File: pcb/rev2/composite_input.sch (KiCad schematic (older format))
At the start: 19 parts, among them IC28 TVP5150AM1PBS, X1 XTAL_12MHZ_TXC_7A-14.31818MAA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

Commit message: pcb wip
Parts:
- C29, C30, C31, C52, C59, C83: footprint CAPC1608X87N -> Capacitors SMD:CAPC1608X87N
- C7, C84, C85, C86: footprint CAPC1608X90N -> Capacitors SMD:CAPC1608X90N
- L1, L6: footprint INDC2012X105N -> Inductors SMD:INDC2012X105N
- R19, R32, R33, R4, R48: footprint RESC1608X55N -> Resistors SMD:RESC1608X55N
- X1: footprint XTAL_TXC_7A -> ICs And Semiconductors SMD:XTAL_TXC_7A
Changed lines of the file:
@@
 F 0 "R19" H 2050 1697 50  0000 C CNN
 F 1 "R0603_33R_1%_0.1W_100PPM" H 1900 1290 60  0001 L CNN
-F 2 "RESC1608X55N" H 1900 480 60  0001 L CNN
+F 2 "Resistors SMD:RESC1608X55N" H 1900 480 60  0001 L CNN
 F 3 "\\cern.ch\\dfs\\Applications\\Altium\\Datasheets\\R0603_NIC_NRC.pdf" H 1900 1110 60  0001 L CNN
 F 4 "33" H 2050 1606 50  0000 C CNN "~"
@@
 F 0 "R32" V 2404 1660 50  0000 L CNN
 F 1 "R0603_33R_1%_0.1W_100PPM" H 2300 1390 60  0001 L CNN
-F 2 "RESC1608X55N" H 2300 580 60  0001 L CNN
+F 2 "Resistors SMD:RESC1608X55N" H 2300 580 60  0001 L CNN
 F 3 "\\cern.ch\\dfs\\Applications\\Altium\\Datasheets\\R0603_NIC_NRC.pdf" H 2300 1210 60  0001 L CNN
 F 4 "33" V 2495 1660 50  0000 L CNN "~"
@@
 F 0 "C7" H 2600 1747 50  0000 C CNN
 F 1 "CC0603_100NF_100V_10%_X7R" H 2450 1240 60  0001 L CNN
-F 2 "CAPC1608X90N" H 2450 430 60  0001 L CNN
+F 2 "Capacitors SMD:CAPC1608X90N" H 2450 430 60  0001 L CNN
 F 3 "\\cern.ch\\dfs\\Applications\\Altium\\Datasheets\\CC0603_MURATA_GRM188R72A104KA35D.pdf" H 2450 1060 60  0001 L CNN
 F 4 "100nF" H 2600 1656 50  0000 C CNN "~"
@@
 F 0 "R33" H 4400 3297 50  0000 C CNN
 F 1 "R0603_3K3_1%_0.1W_100PPM" H 4250 2890 60  0001 L CNN
-F 2 "RESC1608X55N" H 4250 2080 60  0001 L CNN
+F 2 "Resistors SMD:RESC1608X55N" H 4250 2080 60  0001 L CNN
 F 3 "\\cern.ch\\dfs\\Applications\\Altium\\Datasheets\\R0603_NIC_NRC.pdf" H 4250 2710 60  0001 L CNN
 F 4 "3k3" H 4400 3206 50  0000 C CNN "~"
@@
 F 0 "R4" H 4400 3050 50  0000 C CNN
 F 1 "R0603_3K3_1%_0.1W_100PPM" H 4250 2990 60  0001 L CNN
-F 2 "RESC1608X55N" H 4250 2180 60  0001 L CNN
+F 2 "Resistors SMD:RESC1608X55N" H 4250 2180 60  0001 L CNN
 F 3 "\\cern.ch\\dfs\\Applications\\Altium\\Datasheets\\R0603_NIC_NRC.pdf" H 4250 2810 60  0001 L CNN
 F 4 "3k3" H 4400 2950 50  0000 C CNN "~"
@@
 F 0 "C31" V 3404 3710 50  0000 L CNN
 F 1 "CC0603_22PF_50V_5%_NP0" H 3300 3340 60  0001 L CNN
-F 2 "CAPC1608X87N" H 3300 2530 60  0001 L CNN
+F 2 "Capacitors SMD:CAPC1608X87N" H 3300 2530 60  0001 L CNN
 F 3 "\\cern.ch\\dfs\\Applications\\Altium\\Datasheets\\CC0603_NP0_PHYCOMP.pdf" H 3300 3160 60  0001 L CNN
 F 4 "22pF" V 3495 3710 50  0000 L CNN "~"
@@
 F 0 "C59" V 2954 3710 50  0000 L CNN
 F 1 "CC0603_22PF_50V_5%_NP0" H 2850 3340 60  0001 L CNN
-F 2 "CAPC1608X87N" H 2850 2530 60  0001 L CNN
+F 2 "Capacitors SMD:CAPC1608X87N" H 2850 2530 60  0001 L CNN
 F 3 "\\cern.ch\\dfs\\Applications\\Altium\\Datasheets\\CC0603_NP0_PHYCOMP.pdf" H 2850 3160 60  0001 L CNN
 F 4 "22pF" V 3045 3710 50  0000 L CNN "~"
@@
 F 0 "X1" H 2500 3657 50  0000 C CNN
 F 1 "XTAL_12MHZ_TXC_7A-14.31818MAAJ-T" H 2350 3110 60  0001 L CNN
-F 2 "XTAL_TXC_7A" H 2350 2210 60  0001 L CNN
+F 2 "ICs And Semiconductors SMD:XTAL_TXC_7A" H 2350 2210 60  0001 L CNN
 F 3 "\\cern.ch\\dfs\\Applications\\Altium\\Datasheets\\XTAL_TXC_7A.pdf" H 2350 2930 60  0001 L CNN
 F 4 "Value" H 2350 3400 60  0001 C CNN "Fieldname"
@@
 F 0 "C29" V 3604 4960 50  0000 L CNN
 F 1 "CC0603_1UF_50V_10%_X5R" H 3500 4590 60  0001 L CNN
-F 2 "CAPC1608X87N" H 3500 3780 60  0001 L CNN
+F 2 "Capacitors SMD:CAPC1608X87N" H 3500 3780 60  0001 L CNN
 F 3 "\\cern.ch\\dfs\\Applications\\Altium\\Datasheets\\CC0603_X5R_TDK_C.pdf" H 3500 4410 60  0001 L CNN
 F 4 "1uF" V 3695 4960 50  0000 L CNN "~"
@@
 F 0 "C30" H 4050 4453 50  0000 C CNN
 F 1 "CC0603_1UF_50V_10%_X5R" H 3900 4440 60  0001 L CNN
-F 2 "CAPC1608X87N" H 3900 3630 60  0001 L CNN
+F 2 "Capacitors SMD:CAPC1608X87N" H 3900 3630 60  0001 L CNN
 F 3 "\\cern.ch\\dfs\\Applications\\Altium\\Datasheets\\CC0603_X5R_TDK_C.pdf" H 3900 4260 60  0001 L CNN
 F 4 "1uF" H 4050 4544 50  0000 C CNN "~"
@@
 F 0 "C52" V 4146 5040 50  0000 R CNN
 F 1 "CC0603_1UF_50V_10%_X5R" H 3950 4890 60  0001 L CNN
-F 2 "CAPC1608X87N" H 3950 4080 60  0001 L CNN
+F 2 "Capacitors SMD:CAPC1608X87N" H 3950 4080 60  0001 L CNN
 F 3 "\\cern.ch\\dfs\\Applications\\Altium\\Datasheets\\CC0603_X5R_TDK_C.pdf" H 3950 4710 60  0001 L CNN
 F 4 "1uF" V 4055 5040 50  0000 R CNN "~"
@@
 F 0 "L1" H 5900 6317 50  0000 C CNN
 F 1 "IND0805_MURATA_BLM21PG221SN1D" H 5750 5910 60  0001 L CNN
-F 2 "INDC2012X105N" H 5750 5100 60  0001 L CNN
+F 2 "Inductors SMD:INDC2012X105N" H 5750 5100 60  0001 L CNN
 F 3 "\\cern.ch\\dfs\\Applications\\Altium\\Datasheets\\IND0805_MURATA_BLM21P.pdf" H 5750 5730 60  0001 L CNN
 F 4 "220R@100MHz" H 5900 6226 50  0000 C CNN "~"
@@
 F 0 "L6" H 5900 6617 50  0000 C CNN
 F 1 "IND0805_MURATA_BLM21PG221SN1D" H 5750 6210 60  0001 L CNN
-F 2 "INDC2012X105N" H 5750 5400 60  0001 L CNN
+F 2 "Inductors SMD:INDC2012X105N" H 5750 5400 60  0001 L CNN
 F 3 "\\cern.ch\\dfs\\Applications\\Altium\\Datasheets\\IND0805_MURATA_BLM21P.pdf" H 5750 6030 60  0001 L CNN
 F 4 "220R@100MHz" H 5900 6526 50  0000 C CNN "~"
@@
 F 0 "C83" V 3554 6310 50  0000 L CNN
 F 1 "CC0603_1UF_50V_10%_X5R" H 3450 5940 60  0001 L CNN
-F 2 "CAPC1608X87N" H 3450 5130 60  0001 L CNN
+F 2 "Capacitors SMD:CAPC1608X87N" H 3450 5130 60  0001 L CNN
 F 3 "\\cern.ch\\dfs\\Applications\\Altium\\Datasheets\\CC0603_X5R_TDK_C.pdf" H 3450 5760 60  0001 L CNN
 F 4 "1uF" V 3645 6310 50  0000 L CNN "~"
@@
 F 0 "C84" V 3954 6310 50  0000 L CNN
 F 1 "CC0603_100NF_100V_10%_X7R" H 3850 5940 60  0001 L CNN
-F 2 "CAPC1608X90N" H 3850 5130 60  0001 L CNN
+F 2 "Capacitors SMD:CAPC1608X90N" H 3850 5130 60  0001 L CNN
 F 3 "\\cern.ch\\dfs\\Applications\\Altium\\Datasheets\\CC0603_MURATA_GRM188R72A104KA35D.pdf" H 3850 5760 60  0001 L CNN
 F 4 "100nF" V 4045 6310 50  0000 L CNN "~"
@@
 F 0 "C85" V 4454 6310 50  0000 L CNN
 F 1 "CC0603_100NF_100V_10%_X7R" H 4350 5940 60  0001 L CNN
-F 2 "CAPC1608X90N" H 4350 5130 60  0001 L CNN
+F 2 "Capacitors SMD:CAPC1608X90N" H 4350 5130 60  0001 L CNN
 F 3 "\\cern.ch\\dfs\\Applications\\Altium\\Datasheets\\CC0603_MURATA_GRM188R72A104KA35D.pdf" H 4350 5760 60  0001 L CNN
 F 4 "100nF" V 4545 6310 50  0000 L CNN "~"
@@
 F 0 "C86" V 4904 6310 50  0000 L CNN
 F 1 "CC0603_100NF_100V_10%_X7R" H 4800 5940 60  0001 L CNN
-F 2 "CAPC1608X90N" H 4800 5130 60  0001 L CNN
+F 2 "Capacitors SMD:CAPC1608X90N" H 4800 5130 60  0001 L CNN
 F 3 "\\cern.ch\\dfs\\Applications\\Altium\\Datasheets\\CC0603_MURATA_GRM188R72A104KA35D.pdf" H 4800 5760 60  0001 L CNN
 F 4 "100nF" V 4995 6310 50  0000 L CNN "~"
@@
 F 0 "R48" V 7504 4210 50  0000 L CNN
 F 1 "R0603_3K3_1%_0.1W_100PPM" H 7400 3940 60  0001 L CNN
-F 2 "RESC1608X55N" H 7400 3130 60  0001 L CNN
+F 2 "Resistors SMD:RESC1608X55N" H 7400 3130 60  0001 L CNN
 F 3 "\\cern.ch\\dfs\\Applications\\Altium\\Datasheets\\R0603_NIC_NRC.pdf" H 7400 3760 60  0001 L CNN
 F 4 "3k3" V 7595 4210 50  0000 L CNN "~"

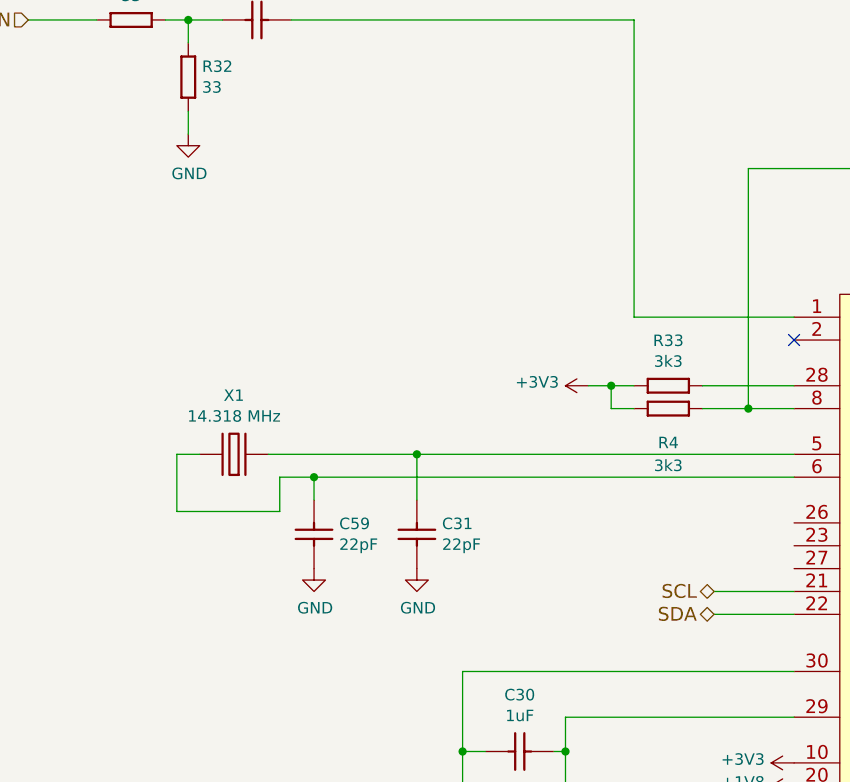
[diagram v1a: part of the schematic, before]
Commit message: Completed port to KiCad, passes DRC+LVS. NOT MANUFACTURED.
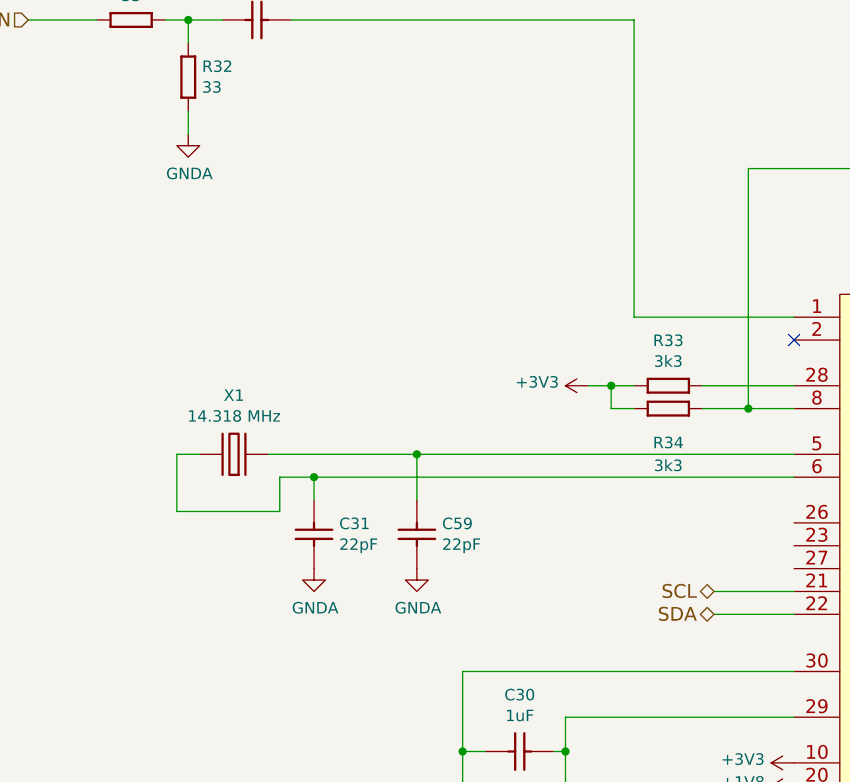
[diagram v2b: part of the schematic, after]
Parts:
- IC28: footprint (none) -> dsi_shield:TSQFP50P700X700-32L
- renumbered R4 to R34
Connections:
- net GND: no longer C31.2, C59.2, R32.2
- net GNDA: now also C31.2, C59.2, R32.2
- net at IC28.5 (XTAL1/OSC), X1.2 (OSC2): now also C59.1; no longer C31.1
- net at IC28.6 (XTAL2), X1.1 (OSC1): now also C31.1; no longer C59.1
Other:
- moved on the sheet: C31, C59
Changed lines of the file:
@@
 F 0 "IC28" H 5950 2773 50  0000 C CNN
 F 1 "TVP5150AM1PBS" H 5150 2800 60  0001 L CNN
-F 2 "" H 5150 2700 60  0001 C CNN
+F 2 "dsi_shield:TSQFP50P700X700-32L" H 5150 2700 60  0001 C CNN
 F 3 "" H 5150 2700 60  0001 C CNN
 F 4 "Value" H 5150 2700 60  0001 C CNN "Fieldname"
@@
 $EndComp
 $Comp
-L GND #PWR0110
-U 1 1 599061B2
-P 2300 2000
-F 0 "#PWR0110" H 2300 1750 50  0001 C CNN
-F 1 "GND" H 2305 1827 50  0000 C CNN
-F 2 "" H 2300 2000 50  0001 C CNN
-F 3 "" H 2300 2000 50  0001 C CNN
-	1    2300 2000
-	1    0    0    -1
-$EndComp
-$Comp
 L CC0603_100NF_100V_10%_X7R C7
 U 1 1 59906E21
@@
 $EndComp
 $Comp
-L R0603_3K3_1%_0.1W_100PPM R4
+L R0603_3K3_1%_0.1W_100PPM R34
 U 1 1 5990925B
 P 4250 3200
-F 0 "R4" H 4400 3050 50  0000 C CNN
+F 0 "R34" H 4400 3050 50  0000 C CNN
 F 1 "R0603_3K3_1%_0.1W_100PPM" H 4250 2990 60  0001 L CNN
 F 2 "Resistors SMD:RESC1608X55N" H 4250 2180 60  0001 L CNN
@@
 L CC0603_22PF_50V_5%_NP0 C31
 U 1 1 5990B552
+P 2850 3600
+F 0 "C31" V 2954 3710 50  0000 L CNN
+F 1 "CC0603_22PF_50V_5%_NP0" H 2850 3340 60  0001 L CNN
+F 2 "Capacitors SMD:CAPC1608X87N" H 2850 2530 60  0001 L CNN
+F 3 "\\cern.ch\\dfs\\Applications\\Altium\\Datasheets\\CC0603_NP0_PHYCOMP.pdf" H 2850 3160 60  0001 L CNN
+F 4 "22pF" V 3045 3710 50  0000 L CNN "~"
+F 5 "CC0603_22PF_50V_5%_NP0" H 2850 3070 60  0001 L CNN "Part Number"
+F 6 "Capacitor - non polarized" H 2850 2980 60  0001 L CNN "Library Ref"
+F 7 "SchLib\\Capacitors.SchLib" H 2850 2890 60  0001 L CNN "Library Path"
+F 8 "=Value" H 2850 2800 60  0001 L CNN "Comment"
+F 9 "Standard" H 2850 2710 60  0001 L CNN "Component Kind"
+F 10 "Standard" H 2850 2620 60  0001 L CNN "Component Type"
+F 11 "2.0000000000000000e+00" H 2850 2440 60  0001 L CNN "Pin Count"
+F 12 "PcbLib\\Capacitors SMD.PcbLib" H 2850 2350 60  0001 L CNN "Footprint Path"
+F 13 "CAPC1608X87N" H 2850 2260 60  0001 L CNN "Footprint Ref"
+F 14 "~~" H 2850 2170 60  0001 L CNN "PackageDescription"
+F 15 "22pF" H 2850 2080 60  0001 L CNN "Val"
+F 16 "Preferred" H 2850 1990 60  0001 L CNN "Status"
+F 17 "~~" H 2850 1900 60  0001 L CNN "Status Comment"
+F 18 "50V" H 2850 1810 60  0001 L CNN "Voltage"
+F 19 "C0G/NP0" H 2850 1720 60  0001 L CNN "TC"
+F 20 "±5%" H 2850 1630 60  0001 L CNN "Tolerance"
+F 21 "SMD Multilayer Chip Ceramic Capacitor" H 2850 1540 60  0001 L CNN "Part Description"
+F 22 "GENERIC" H 2850 1450 60  0001 L CNN "Manufacturer"
+F 23 "CC0603_22PF_50V_5%_NP0" H 2850 1360 60  0001 L CNN "Manufacturer Part Number"
+F 24 "0603" H 2850 1270 60  0001 L CNN "Case"
+F 25 "Yes" H 2850 1180 60  0001 L CNN "Mounted"
+F 26 "No" H 2850 1090 60  0001 L CNN "Socket"
+F 27 "Yes" H 2850 1000 60  0001 L CNN "SMD"
+F 28 "~~" H 2850 910 60  0001 L CNN "PressFit"
+F 29 "No" H 2850 820 60  0001 L CNN "Sense"
+F 30 "~~" H 2850 730 60  0001 L CNN "Sense Comment"
+F 31 "~~" H 2850 640 60  0001 L CNN "ComponentHeight"
+F 32 "PHYCOMP" H 2850 550 60  0001 L CNN "Manufacturer1 Example"
+F 33 "223886715229" H 2850 460 60  0001 L CNN "Manufacturer1 Part Number"
+F 34 "0.87mm" H 2850 370 60  0001 L CNN "Manufacturer1 ComponentHeight"
+F 35 "\\cern.ch\\dfs\\Applications\\Altium\\Datasheets\\CC0603_NP0_PHYCOMP.pdf" H 2850 280 60  0001 L CNN "HelpURL"
+F 36 "CERN DEM JLC" H 2850 190 60  0001 L CNN "Author"
+F 37 "12/03/07 00:00:00" H 2850 100 60  0001 L CNN "CreateDate"
+F 38 "12/03/07 00:00:00" H 2850 10  60  0001 L CNN "LatestRevisionDate"
+F 39 "Capacitors SMD" H 2850 -80 60  0001 L CNN "Library Name"
+F 40 "This work is licensed under the Creative Commons CC-BY-SA 4.0 License. To the extent that circuit schematics that use Licensed Material can be considered to be ‘Adapted Material’, then the copyright holder waives article 3.b of the license with respect to these schematics." H 2850 -170 60  0001 L CNN "License"
+	1    2850 3600
+	0    1    1    0
+$EndComp
+$Comp
+L CC0603_22PF_50V_5%_NP0 C59
+U 1 1 5990B6BB
 P 3300 3600
-F 0 "C31" V 3404 3710 50  0000 L CNN
+F 0 "C59" V 3404 3710 50  0000 L CNN
 F 1 "CC0603_22PF_50V_5%_NP0" H 3300 3340 60  0001 L CNN
 F 2 "Capacitors SMD:CAPC1608X87N" H 3300 2530 60  0001 L CNN
@@
 	1    3300 3600
 	0    1    1    0
-$EndComp
-$Comp
-L CC0603_22PF_50V_5%_NP0 C59
-U 1 1 5990B6BB
-P 2850 3600
-F 0 "C59" V 2954 3710 50  0000 L CNN
-F 1 "CC0603_22PF_50V_5%_NP0" H 2850 3340 60  0001 L CNN
-F 2 "Capacitors SMD:CAPC1608X87N" H 2850 2530 60  0001 L CNN
-F 3 "\\cern.ch\\dfs\\Applications\\Altium\\Datasheets\\CC0603_NP0_PHYCOMP.pdf" H 2850 3160 60  0001 L CNN
-F 4 "22pF" V 3045 3710 50  0000 L CNN "~"
-F 5 "CC0603_22PF_50V_5%_NP0" H 2850 3070 60  0001 L CNN "Part Number"
-F 6 "Capacitor - non polarized" H 2850 2980 60  0001 L CNN "Library Ref"
-F 7 "SchLib\\Capacitors.SchLib" H 2850 2890 60  0001 L CNN "Library Path"
-F 8 "=Value" H 2850 2800 60  0001 L CNN "Comment"
-F 9 "Standard" H 2850 2710 60  0001 L CNN "Component Kind"
-F 10 "Standard" H 2850 2620 60  0001 L CNN "Component Type"
-F 11 "2.0000000000000000e+00" H 2850 2440 60  0001 L CNN "Pin Count"
-F 12 "PcbLib\\Capacitors SMD.PcbLib" H 2850 2350 60  0001 L CNN "Footprint Path"
-F 13 "CAPC1608X87N" H 2850 2260 60  0001 L CNN "Footprint Ref"
-F 14 "~~" H 2850 2170 60  0001 L CNN "PackageDescription"
-F 15 "22pF" H 2850 2080 60  0001 L CNN "Val"
-F 16 "Preferred" H 2850 1990 60  0001 L CNN "Status"
-F 17 "~~" H 2850 1900 60  0001 L CNN "Status Comment"
-F 18 "50V" H 2850 1810 60  0001 L CNN "Voltage"
-F 19 "C0G/NP0" H 2850 1720 60  0001 L CNN "TC"
-F 20 "±5%" H 2850 1630 60  0001 L CNN "Tolerance"
-F 21 "SMD Multilayer Chip Ceramic Capacitor" H 2850 1540 60  0001 L CNN "Part Description"
-F 22 "GENERIC" H 2850 1450 60  0001 L CNN "Manufacturer"
-F 23 "CC0603_22PF_50V_5%_NP0" H 2850 1360 60  0001 L CNN "Manufacturer Part Number"
-F 24 "0603" H 2850 1270 60  0001 L CNN "Case"
-F 25 "Yes" H 2850 1180 60  0001 L CNN "Mounted"
-F 26 "No" H 2850 1090 60  0001 L CNN "Socket"
-F 27 "Yes" H 2850 1000 60  0001 L CNN "SMD"
-F 28 "~~" H 2850 910 60  0001 L CNN "PressFit"
-F 29 "No" H 2850 820 60  0001 L CNN "Sense"
-F 30 "~~" H 2850 730 60  0001 L CNN "Sense Comment"
-F 31 "~~" H 2850 640 60  0001 L CNN "ComponentHeight"
-F 32 "PHYCOMP" H 2850 550 60  0001 L CNN "Manufacturer1 Example"
-F 33 "223886715229" H 2850 460 60  0001 L CNN "Manufacturer1 Part Number"
-F 34 "0.87mm" H 2850 370 60  0001 L CNN "Manufacturer1 ComponentHeight"
-F 35 "\\cern.ch\\dfs\\Applications\\Altium\\Datasheets\\CC0603_NP0_PHYCOMP.pdf" H 2850 280 60  0001 L CNN "HelpURL"
-F 36 "CERN DEM JLC" H 2850 190 60  0001 L CNN "Author"
-F 37 "12/03/07 00:00:00" H 2850 100 60  0001 L CNN "CreateDate"
-F 38 "12/03/07 00:00:00" H 2850 10  60  0001 L CNN "LatestRevisionDate"
-F 39 "Capacitors SMD" H 2850 -80 60  0001 L CNN "Library Name"
-F 40 "This work is licensed under the Creative Commons CC-BY-SA 4.0 License. To the extent that circuit schematics that use Licensed Material can be considered to be ‘Adapted Material’, then the copyright holder waives article 3.b of the license with respect to these schematics." H 2850 -170 60  0001 L CNN "License"
-	1    2850 3600
-	0    1    1    0
-$EndComp
-$Comp
-L GND #PWR0112
-U 1 1 5990B96D
-P 2850 3900
-F 0 "#PWR0112" H 2850 3650 50  0001 C CNN
-F 1 "GND" H 2855 3727 50  0000 C CNN
-F 2 "" H 2850 3900 50  0001 C CNN
-F 3 "" H 2850 3900 50  0001 C CNN
-	1    2850 3900
-	1    0    0    -1
-$EndComp
-$Comp
-L GND #PWR0113
-U 1 1 5990BA01
-P 3300 3900
-F 0 "#PWR0113" H 3300 3650 50  0001 C CNN
-F 1 "GND" H 3305 3727 50  0000 C CNN
-F 2 "" H 3300 3900 50  0001 C CNN
-F 3 "" H 3300 3900 50  0001 C CNN
-	1    3300 3900
-	1    0    0    -1
 $EndComp
 $Comp
@@
 Text Notes 8525 7500 2    60   ~ 0
 Composite input/decoder
+$Comp
+L GNDA #PWR0110
+U 1 1 599E49EF
+P 2300 2000
+F 0 "#PWR0110" H 2300 1750 50  0001 C CNN
+F 1 "GNDA" H 2305 1827 50  0000 C CNN
+F 2 "" H 2300 2000 50  0001 C CNN
+F 3 "" H 2300 2000 50  0001 C CNN
+	1    2300 2000
+	1    0    0    -1
+$EndComp
+$Comp
+L GNDA #PWR0112
+U 1 1 599EEF10
+P 2850 3900
+F 0 "#PWR0112" H 2850 3650 50  0001 C CNN
+F 1 "GNDA" H 2855 3727 50  0000 C CNN
+F 2 "" H 2850 3900 50  0001 C CNN
+F 3 "" H 2850 3900 50  0001 C CNN
+	1    2850 3900
+	1    0    0    -1
+$EndComp
+$Comp
+L GNDA #PWR0113
+U 1 1 599EEF41
+P 3300 3900
+F 0 "#PWR0113" H 3300 3650 50  0001 C CNN
+F 1 "GNDA" H 3305 3727 50  0000 C CNN
+F 2 "" H 3300 3900 50  0001 C CNN
+F 3 "" H 3300 3900 50  0001 C CNN
+	1    3300 3900
+	1    0    0    -1
+$EndComp
 $EndSCHEMATC
